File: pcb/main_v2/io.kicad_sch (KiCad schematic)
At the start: 28 parts, among them IC701 74LVC4T3144PWJ, IC702 74LVC244AD-Q100J, IC703 LTC6992CS6-4#TRMPBF, J701 Conn_01x05_Pin, J702 Conn_01x03_Pin, J703 Conn_01x01_Pin, J704 Conn_01x03_Pin, J705 Conn_01x01_Pin, J706 Conn_01x03_Pin, J707 Conn_01x01_Pin, J708 Conn_01x03_Pin, J709 Conn_01x01_Pin

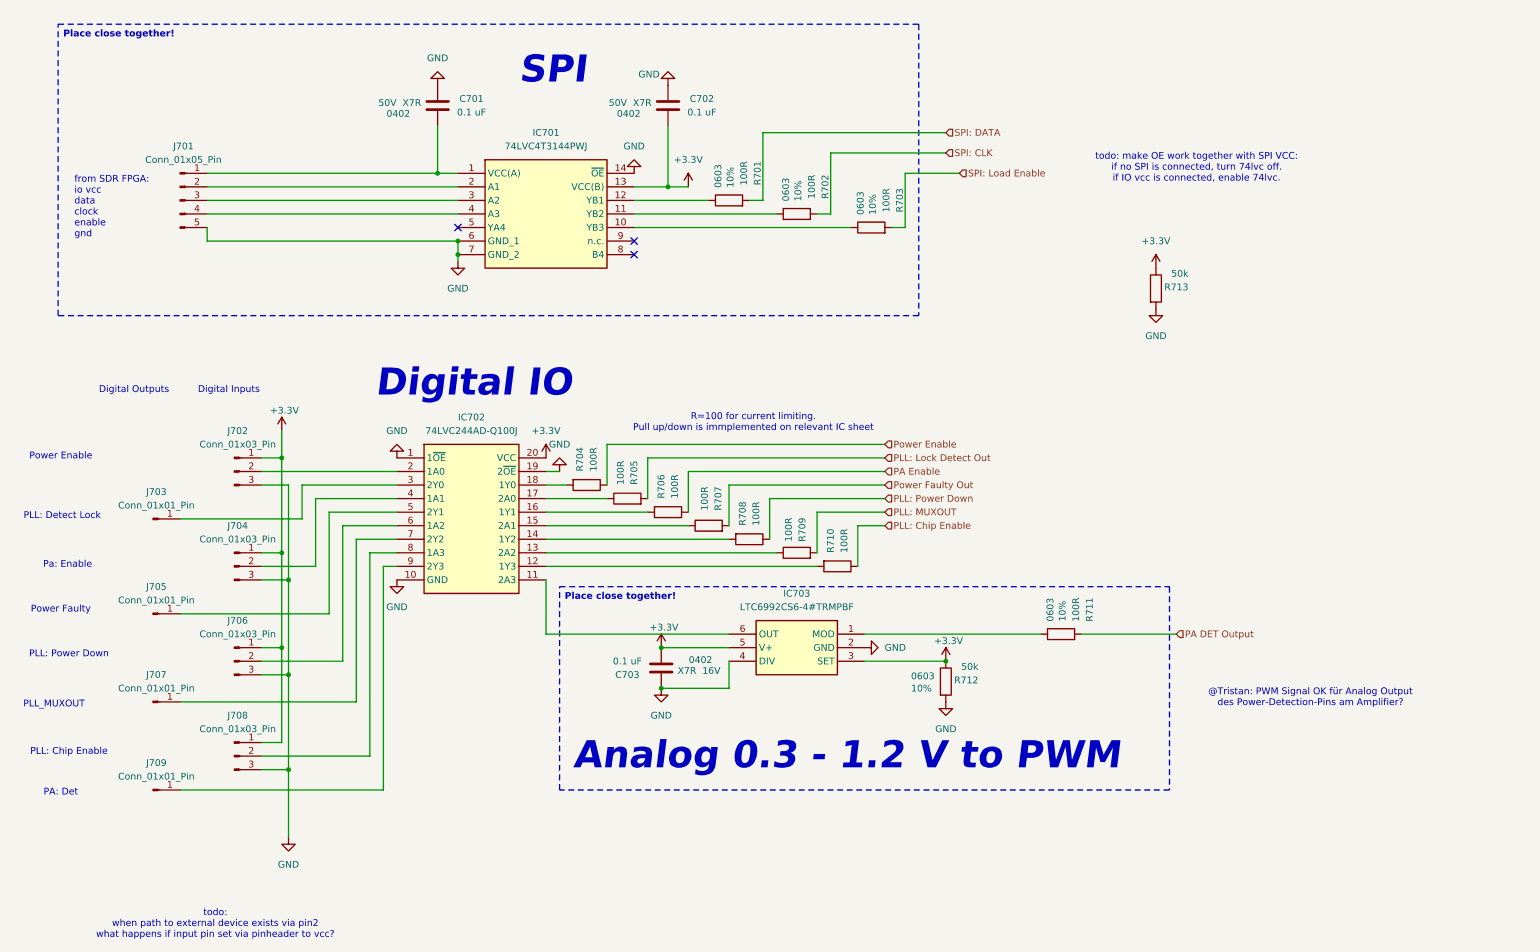
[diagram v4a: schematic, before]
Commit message: updated layout
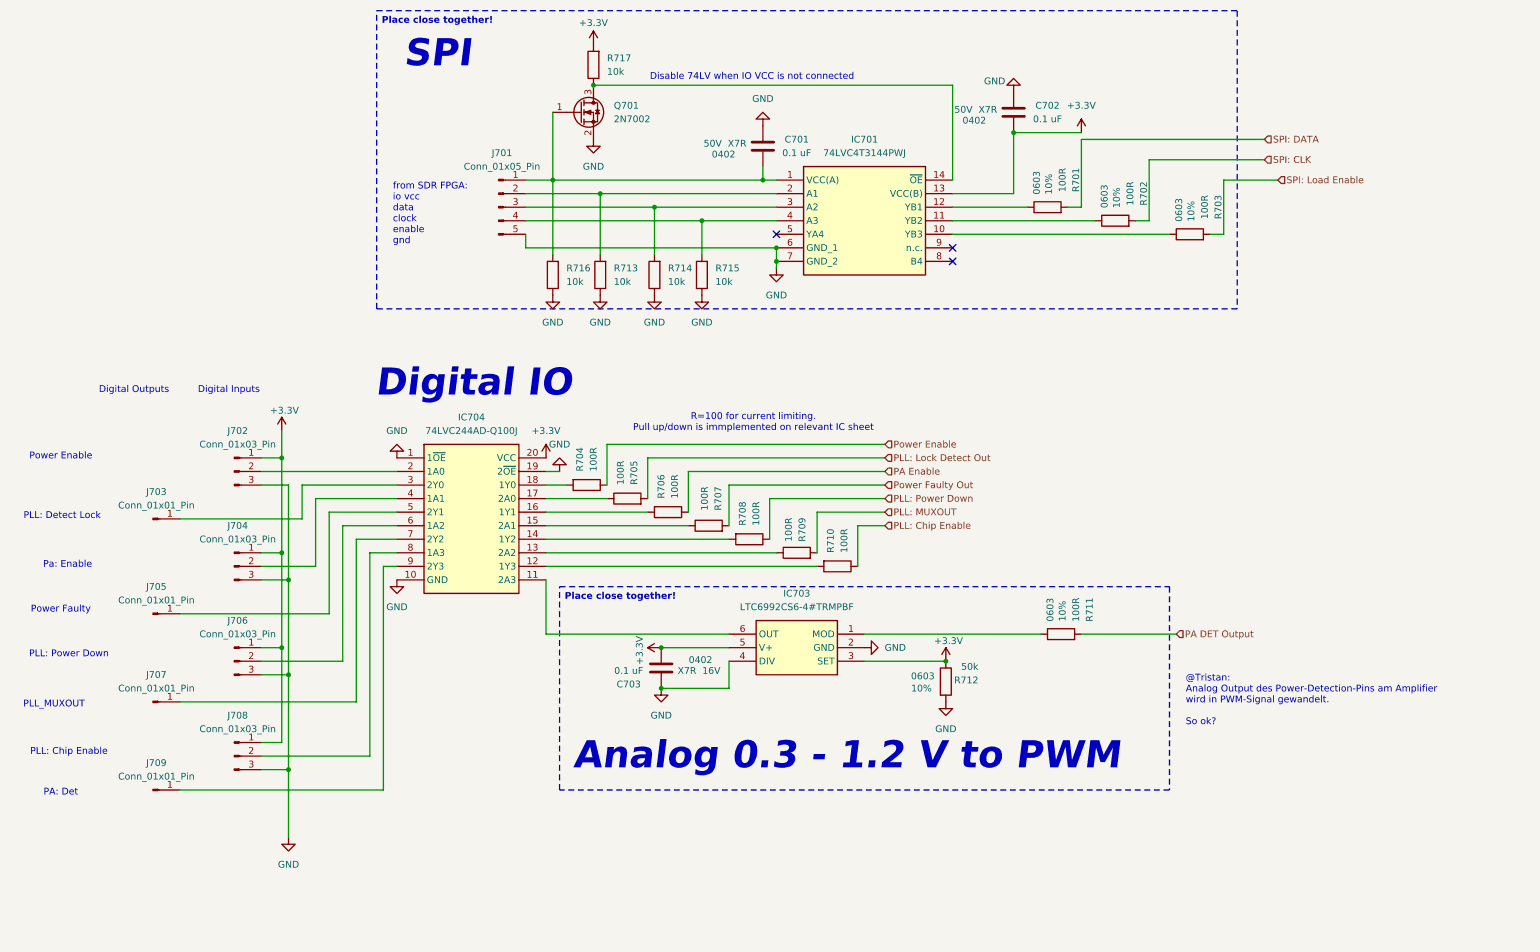
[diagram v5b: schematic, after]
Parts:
- removed IC702: 74LVC244AD-Q100J, My Footprints:SOIC127P1032X265-20N, symbol My Symbols:74LVC244AD-Q100J
- added IC704: 74LVC244AD-Q100J, SOIC127P1032X265-20N, symbol My Symbols:74LVC244AD-Q100J
- added Q701: 2N7002, Package_TO_SOT_SMD:SOT-23, symbol Transistor_FET:2N7002
- added R714, R715, R716, R717: 10k, Resistor_SMD:R_0603_1608Metric, symbol Device:R
- R713: value 50k -> 10k
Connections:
- net +3.3V: now also IC704.20 (VCC), R717.2; no longer R713.1
- net GND: now also R713.1, IC704.1 (1~{OE}), IC704.10 (GND), IC704.19 (2~{OE}), Q701.2 (S), R714.1, R715.1, R716.1; no longer IC701.14 (~{OE}), R713.2
- net at J706.2 (Pin_2): now also IC704.6 (1A2)
- net at J707.1 (Pin_1): now also IC704.7 (2Y2)
- net at C701.1, IC701.1 (VCC(A)), J701.1 (Pin_1): now also Q701.1 (G), R716.2
- net at IC701.2 (A1), J701.2 (Pin_2): now also R713.2
- net at IC701.3 (A2), J701.3 (Pin_3): now also R714.2
- net at IC701.4 (A3), J701.4 (Pin_4): now also R715.2
- net at IC703.6 (OUT): now also IC704.11 (2A3)
- net at R710.2: now also IC704.12 (1Y3)
- net at R709.1: now also IC704.13 (2A2)
- net at R708.2: now also IC704.14 (1Y2)
- net at R707.1: now also IC704.15 (2A1)
- net at R706.2: now also IC704.16 (1Y1)
- net at R705.1: now also IC704.17 (2A0)
- net at R704.2: now also IC704.18 (1Y0)
- net at J702.2 (Pin_2): now also IC704.2 (1A0)
- net at J703.1 (Pin_1): now also IC704.3 (2Y0)
- net at J704.2 (Pin_2): now also IC704.4 (1A1)
- net at J705.1 (Pin_1): now also IC704.5 (2Y1)
- net at J708.2 (Pin_2): now also IC704.8 (1A3)
- net at J709.1 (Pin_1): now also IC704.9 (2Y3)
- new net: IC701.14 (~{OE}), Q701.3 (D), R717.1
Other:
- note added: "@Tristan: Analog Output des Power-Detection-Pins am Amplifier wird in PWM-Signal gewandelt. So ok?"
- note added: "Disable 74LV when IO VCC is not connected"
- note removed: "@Tristan: PWM Signal OK für Analog Output des Power-Detection-Pins am Amplifier?"
- note removed: "todo: make OE work together with SPI VCC: if no SPI is connected, turn 74lvc off. if IO vcc is connected, enable 74lvc."
- note removed: "todo: when path to external device exists via pin2 what happens if input pin set via pinheader to vcc?"
- moved on the sheet: C701, C702, IC701, J701, R701, R702, R703

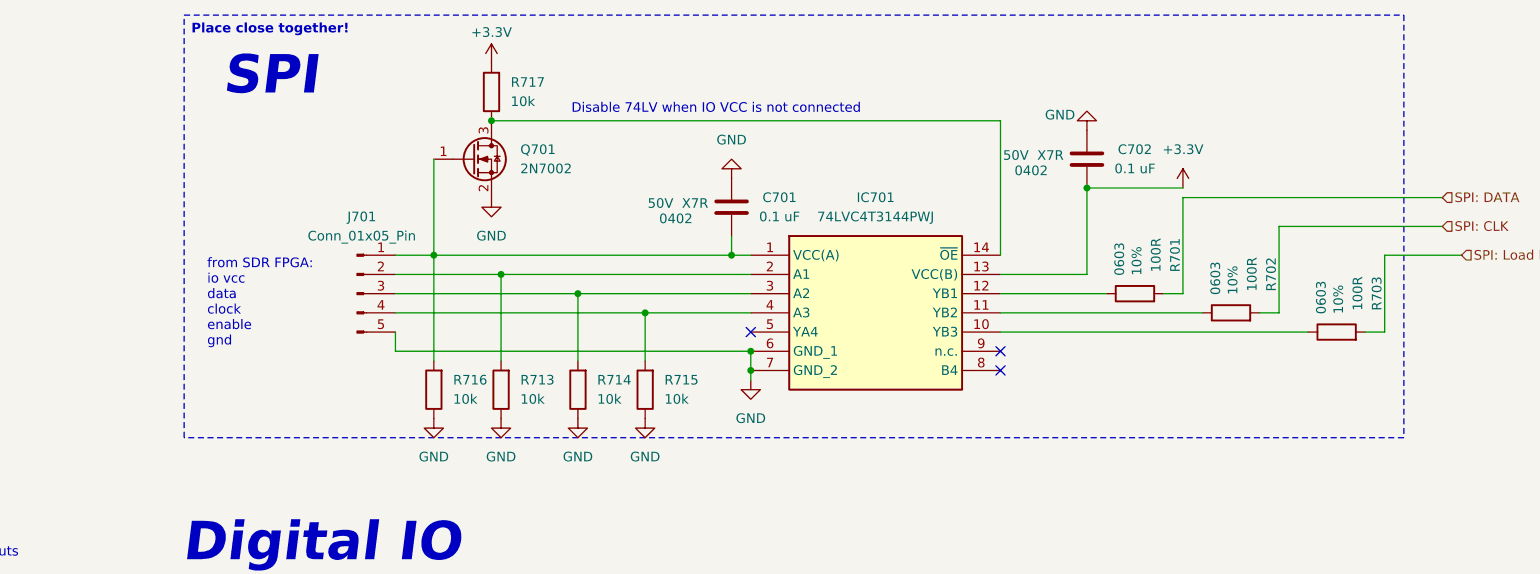
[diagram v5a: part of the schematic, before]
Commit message: updated layout
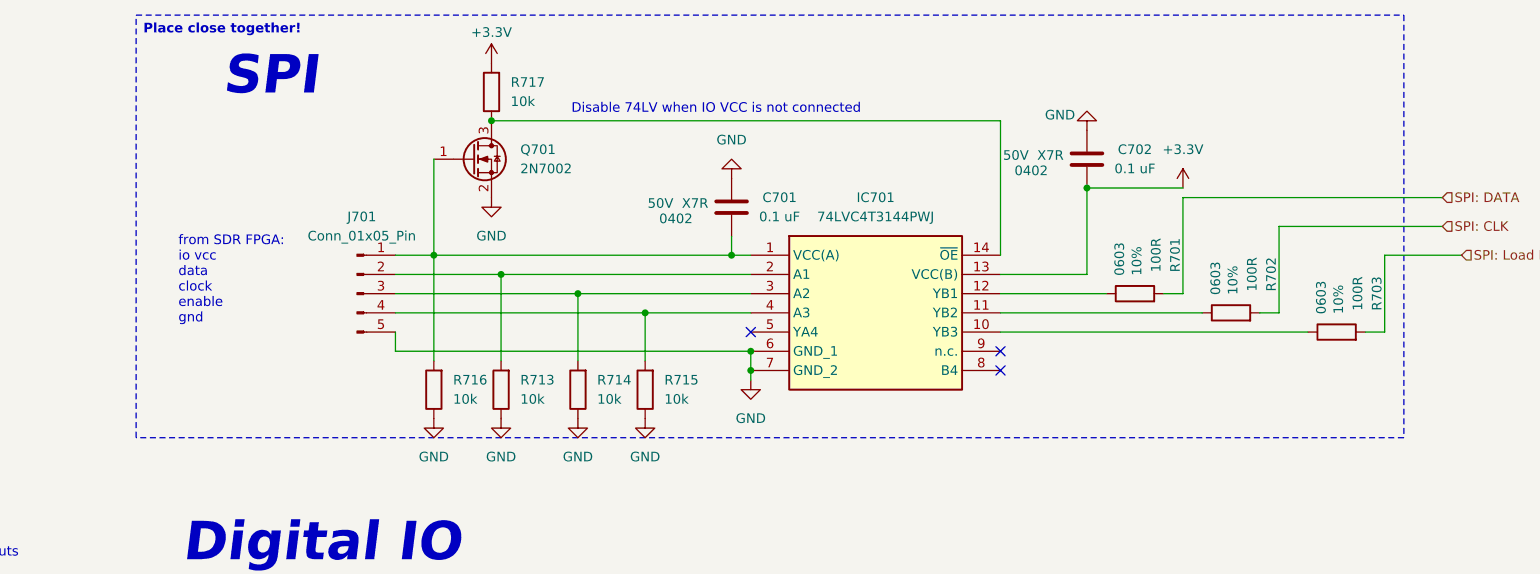
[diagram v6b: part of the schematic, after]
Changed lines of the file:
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@@
 	(text "from SDR FPGA:\nio vcc\ndata\nclock\nenable\ngnd"
 		(exclude_from_sim no)
-		(at 81.788 52.07 0)
+		(at 77.978 49.022 0)
 		(effects
 			(font
@@
 	(text_box "Place close together!"
 		(exclude_from_sim no)
-		(at 78.74 13.97 0)
-		(size 161.29 55.88)
+		(at 72.39 13.97 0)
+		(size 167.64 55.88)
 		(margins 0.9525 0.9525 0.9525 0.9525)
 		(stroke

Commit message: finished layout
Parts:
- IC704: footprint SOIC127P1032X265-20N -> My Footprints:SOIC127P1032X265-20N
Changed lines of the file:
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@@
 			)
 		)
-		(property "Footprint" "SOIC127P1032X265-20N"
+		(property "Footprint" "My Footprints:SOIC127P1032X265-20N"
 			(at 106.68 192.71 0)
 			(hide yes)

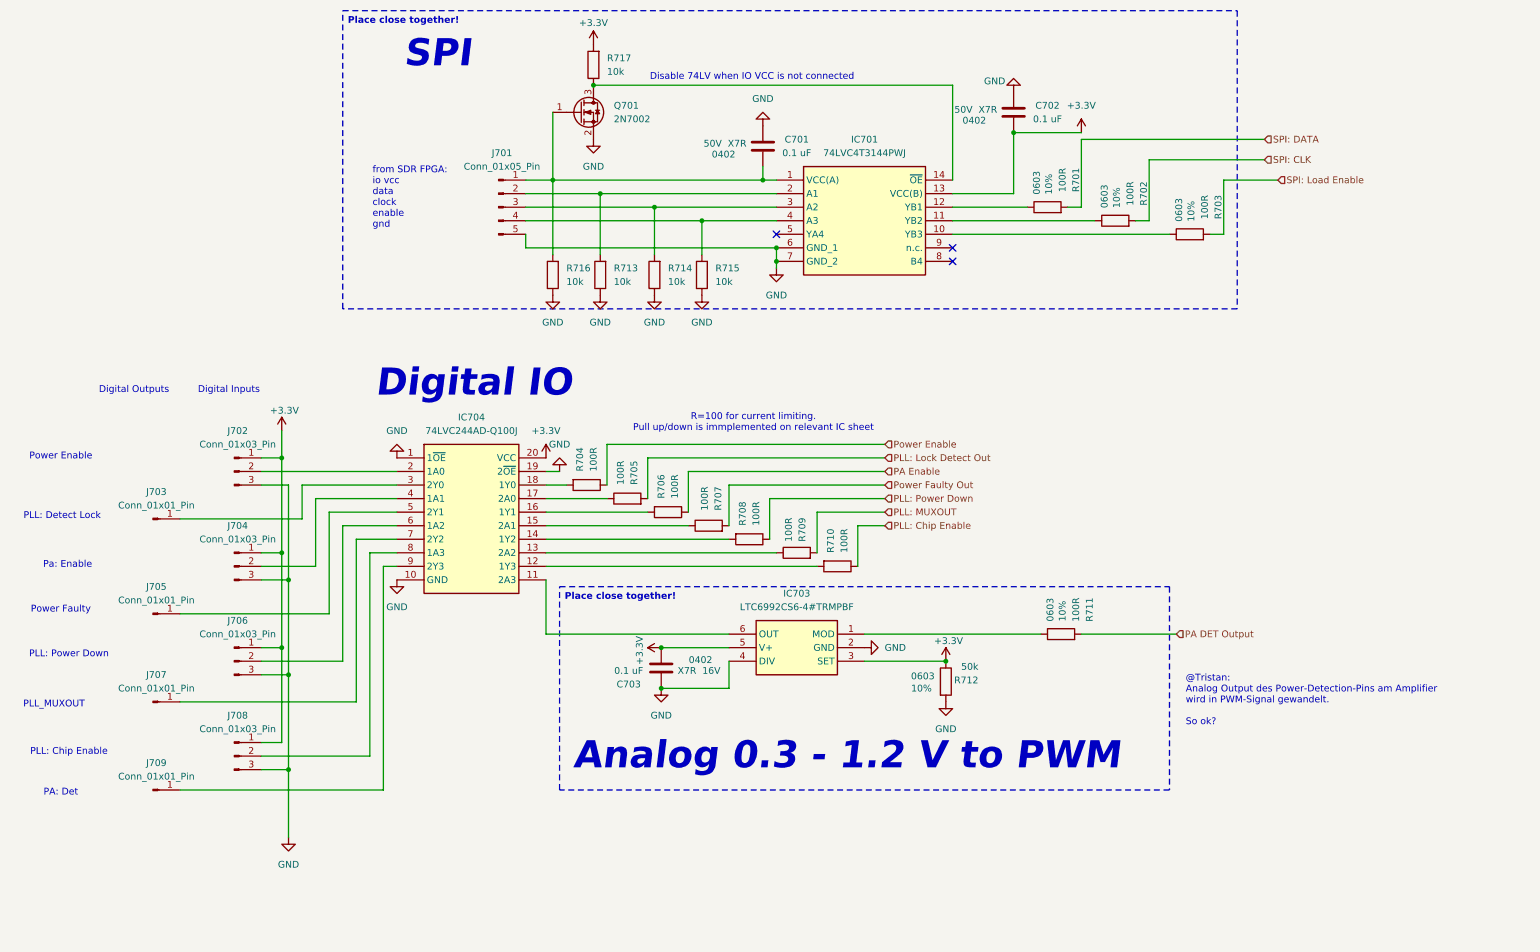
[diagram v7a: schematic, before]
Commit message: updated spi connection
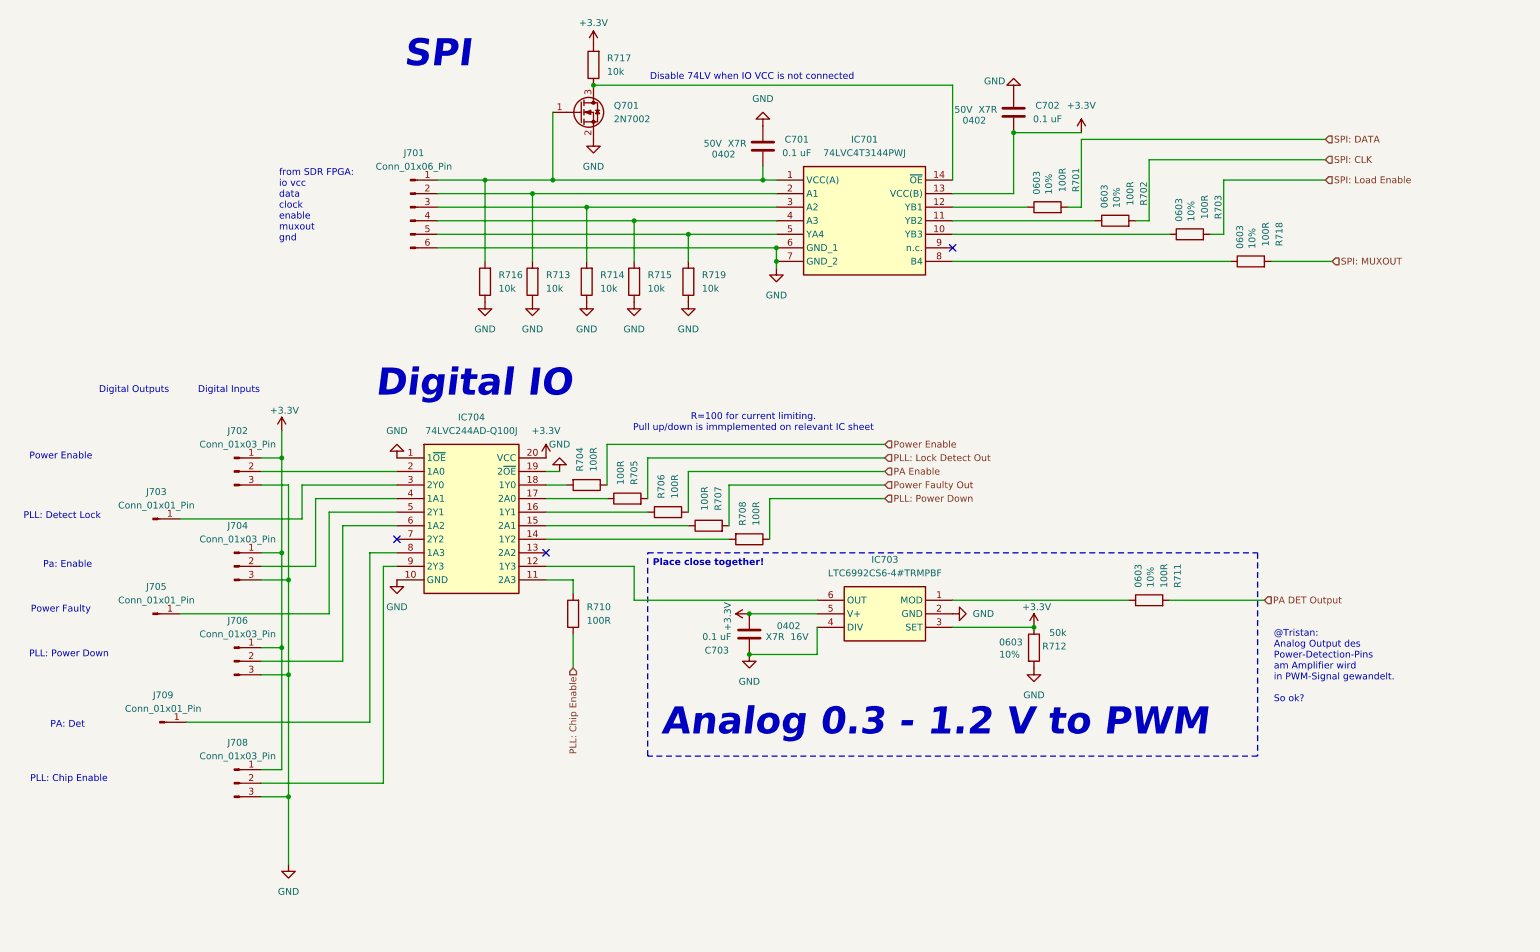
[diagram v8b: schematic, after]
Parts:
- removed J707: Conn_01x01_Pin, Connector_PinHeader_2.54mm:PinHeader_1x01_P2.54mm_Vertical, symbol Connector:Conn_01x01_Pin
- removed R709: 100R, Resistor_SMD:R_0603_1608Metric, symbol Device:R
- added R718: 100R, Resistor_SMD:R_0603_1608Metric, symbol Device:R
- added R719: 10k, Resistor_SMD:R_0603_1608Metric, symbol Device:R
- J701: value Conn_01x05_Pin -> Conn_01x06_Pin; footprint Connector_PinHeader_2.54mm:PinHeader_1x05_P2.54mm_Vertical -> Connector_PinHeader_2.54mm:PinHeader_1x06_P2.54mm_Vertical; symbol Connector:Conn_01x05_Pin -> Connector:Conn_01x06_Pin
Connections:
- net GND: now also J701.6 (Pin_6), R719.1; no longer J701.5 (Pin_5)
- net at R710.2: now also IC704.11 (2A3); no longer IC704.12 (1Y3)
- net at IC703.6 (OUT): now also IC704.12 (1Y3); no longer IC704.11 (2A3)
- net at IC704.8 (1A3): now also J709.1 (Pin_1); no longer J708.2 (Pin_2)
- net at IC704.9 (2Y3): now also J708.2 (Pin_2); no longer J709.1 (Pin_1)
- net at IC701.5 (YA4): now also J701.5 (Pin_5), R719.2
- net at IC701.8 (B4): now also R718.1
- new net SPI: MUXOUT: R718.2
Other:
- note added: "from SDR FPGA: io vcc data clock enable muxout gnd"
- note removed: "PLL_MUXOUT"
- note removed: "from SDR FPGA: io vcc data clock enable gnd"
- moved on the sheet: C703, IC703, J708, J709, R710, R711, R712, R713, R714, R715, R716
